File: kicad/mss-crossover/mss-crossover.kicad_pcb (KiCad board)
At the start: 2 copper layers, 73.7 x 38.1 mm, 40 parts, among them J1 Screw_Terminal_01x02, J2 AVR-ISP, J3 8P8C, J4 8P8C, SW1 FSM4JSMATR, T1 PE-51687, U1 AP7381-33Y, U2 INA180A4, U3 ATtiny85-20S, U4 TLP241A

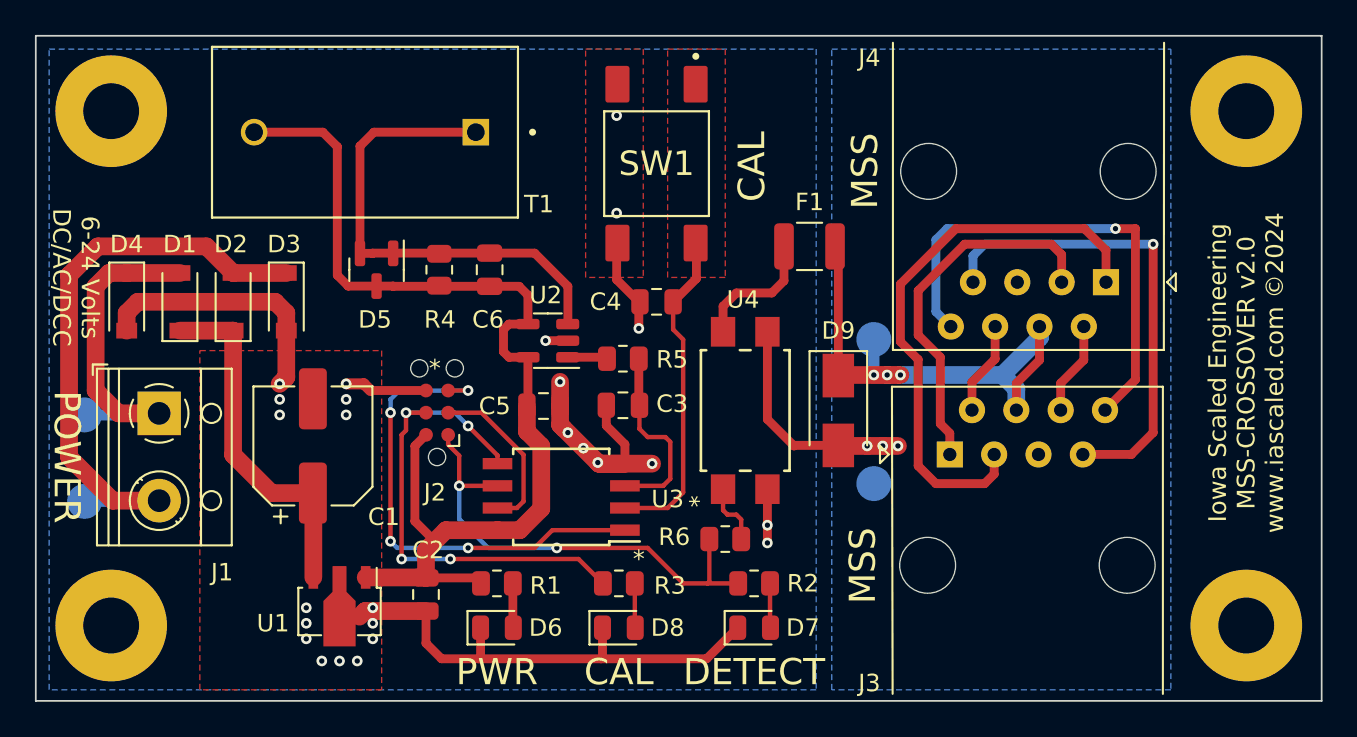
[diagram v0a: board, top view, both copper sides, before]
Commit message: Update footprints for AVR to allow for both narrow/wide SO8s and footprint for CDBMs to allow for more paste
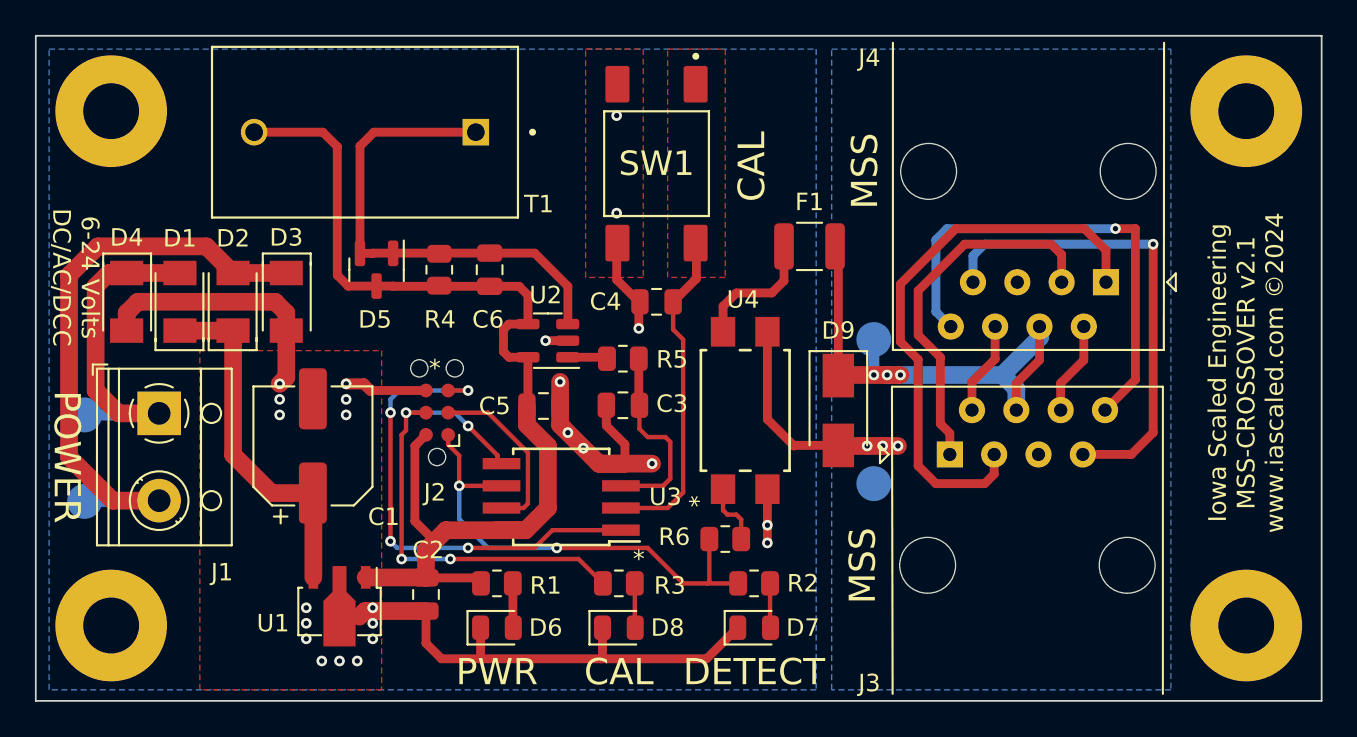
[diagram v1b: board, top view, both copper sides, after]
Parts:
- D1, D2, D3, D4: footprint Diode_SMD:D_SOD-123 -> ISE_Generic:SOD-123T
- U3: footprint Package_SO:SOIC-8W_5.3x5.3mm_P1.27mm -> ISE_Generic:ATMEL_SO8_DUAL
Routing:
- net +3.3V: track 61.5 -> 63.1 mm
- net GND: vias 26 -> 25
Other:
- board text added: "Iowa Scaled Engineering MSS-CROSSOVER v2.1 www.iascaled.com ©2024"
- board text removed: "Iowa Scaled Engineering MSS-CROSSOVER v2.0 www.iascaled.com ©2024"

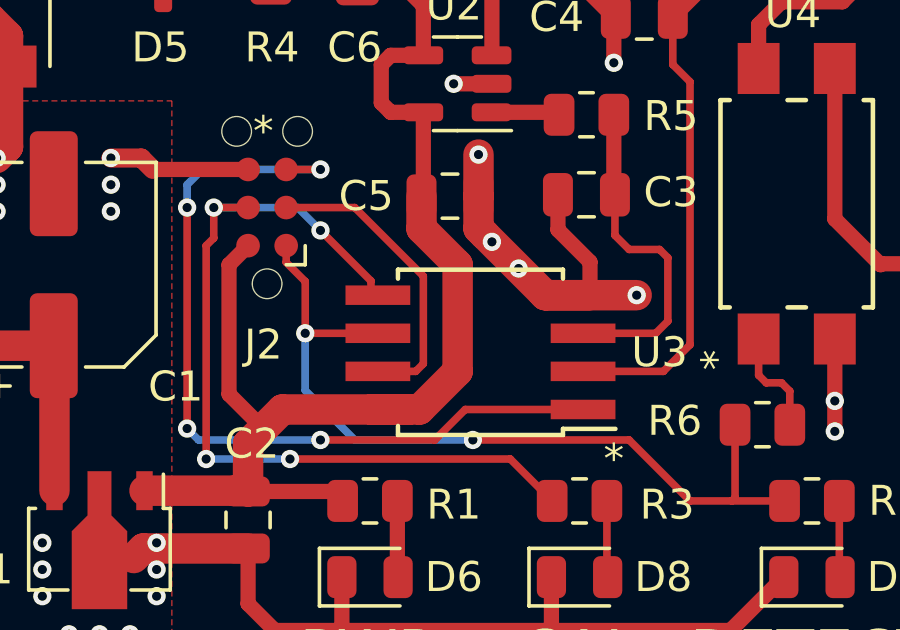
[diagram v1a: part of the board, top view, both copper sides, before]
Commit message: Fix dual footprint SO8
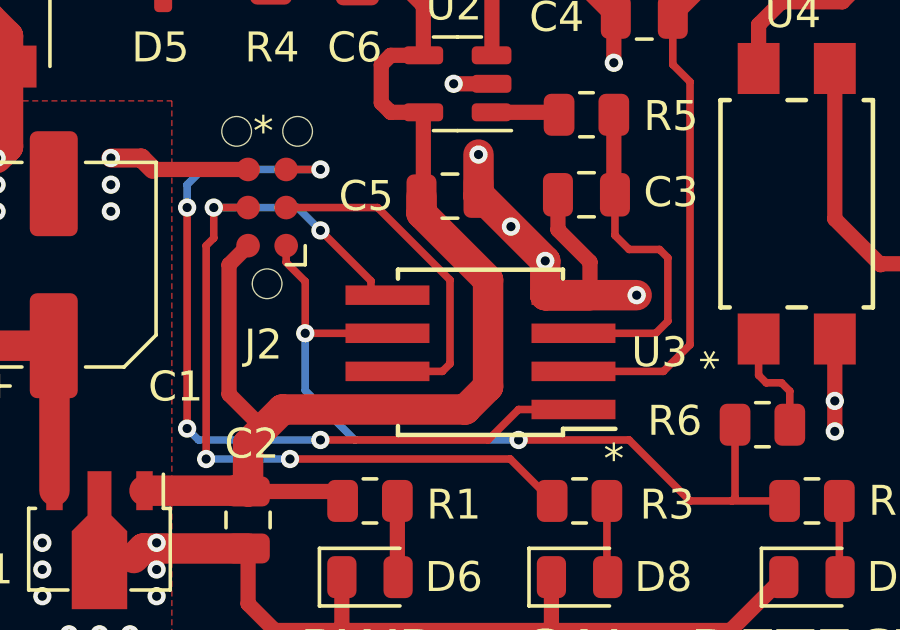
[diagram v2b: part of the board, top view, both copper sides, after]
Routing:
- net Net-(J2-Pad3): track 10.1 -> 12.7 mm
- net +3.3V: track 63.1 -> 63.8 mm

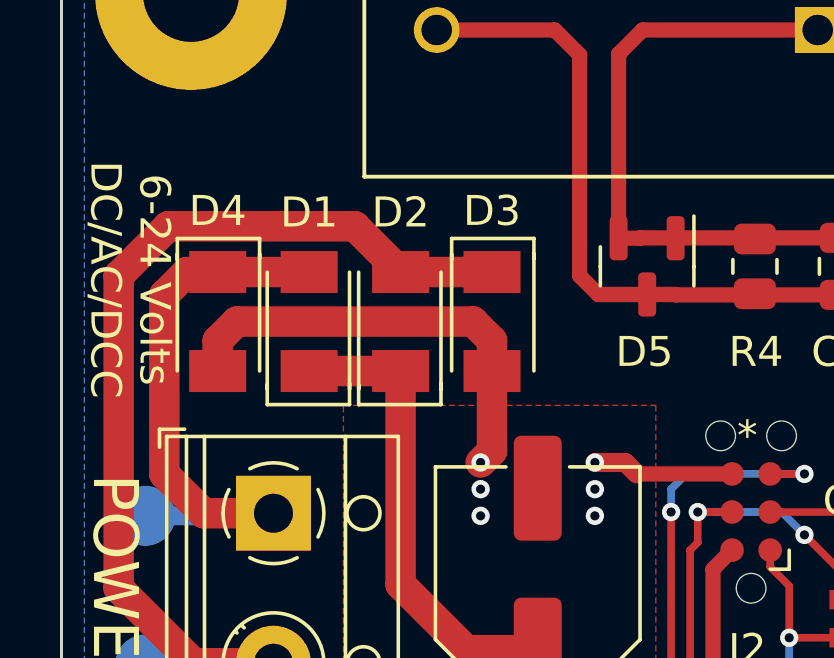
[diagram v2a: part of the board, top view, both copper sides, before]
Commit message: Fix diode spacing to appease McFussyPants
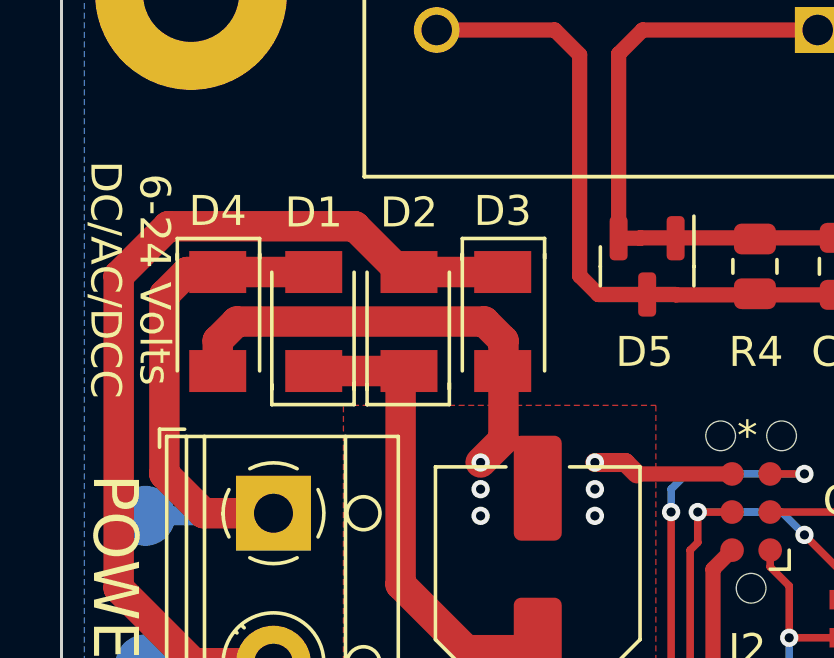
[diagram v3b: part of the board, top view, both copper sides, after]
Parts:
- moved D3 0.36 mm to (40.1, 168.9)
- moved D2 0.28 mm to (37.0, 168.9)
- moved D1 0.15 mm to (33.8, 168.9)
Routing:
- net GND: track 71.5 -> 72.1 mm
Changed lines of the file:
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@@
   )
   (footprint "ISE_Generic:SOD-123T" (layer "F.Cu")
-    (at 36.703 168.91 90)
+    (at 36.9824 168.91 90)
     (descr "SOD-123")
     (tags "SOD-123")
@@
   )
   (footprint "ISE_Generic:SOD-123T" (layer "F.Cu")
-    (at 33.655 168.91 90)
+    (at 33.8074 168.91 90)
     (descr "SOD-123")
     (tags "SOD-123")
@@
   )
   (footprint "ISE_Generic:SOD-123T" (layer "F.Cu")
-    (at 39.751 168.91 -90)
+    (at 40.1066 168.91 -90)
     (descr "SOD-123")
     (tags "SOD-123")
@@
   (segment (start 55.433 174.879) (end 55.433 173.4935) (width 1.016) (layer "F.Cu") (net 2))
   (segment (start 55.499 174.879) (end 57.658 177.038) (width 1.016) (layer "F.Cu") (net 2))
-  (segment (start 39.751 173.228) (end 39.37 173.609) (width 1.016) (layer "F.Cu") (net 2))
   (segment (start 67.31 182.72125) (end 67.31 179.73675) (width 0.508) (layer "F.Cu") (net 2))
   (segment (start 47.752 186.624) (end 47.752 188.468) (width 0.508) (layer "F.Cu") (net 2))
   (segment (start 47.752 188.468) (end 48.641 189.357) (width 0.508) (layer "F.Cu") (net 2))
   (segment (start 58.674 167.64) (end 58.674 165.591) (width 0.508) (layer "F.Cu") (net 2))
-  (segment (start 39.751 170.56) (end 39.751 173.228) (width 1.016) (layer "F.Cu") (net 2))
+  (segment (start 39.497 168.91) (end 40.132 169.545) (width 1.016) (layer "F.Cu") (net 2))
   (segment (start 58.0815 176.0035) (end 59.149 177.071) (width 0.508) (layer "F.Cu") (net 2))
-  (segment (start 31.242 168.91) (end 39.116 168.91) (width 1.016) (layer "F.Cu") (net 2))
   (segment (start 59.944 170.434) (end 59.944 168.976) (width 0.508) (layer "F.Cu") (net 2))
   (segment (start 59.149 177.071) (end 59.149 178.181) (width 0.508) (layer "F.Cu") (net 2))
   (segment (start 47.752 173.99) (end 44.577 173.99) (width 0.508) (layer "F.Cu") (net 2))
   (segment (start 44.262 186.624) (end 43.942 186.944) (width 1.016) (layer "F.Cu") (net 2))
+  (segment (start 31.242 168.91) (end 39.497 168.91) (width 1.016) (layer "F.Cu") (net 2))
   (segment (start 59.944 168.91) (end 58.674 167.64) (width 0.508) (layer "F.Cu") (net 2))
+  (segment (start 40.132 172.847) (end 39.37 173.609) (width 1.016) (layer "F.Cu") (net 2))
   (segment (start 57.658 178.181) (end 59.149 178.181) (width 1.016) (layer "F.Cu") (net 2))
-  (segment (start 30.607 170.56) (end 30.607 169.545) (width 1.016) (layer "F.Cu") (net 2))
   (segment (start 63.8325 189.357) (end 65.6105 187.579) (width 0.508) (layer "F.Cu") (net 2))
-  (segment (start 39.751 169.545) (end 39.751 170.56) (width 1.016) (layer "F.Cu") (net 2))
+  (segment (start 30.607 170.56) (end 30.607 169.545) (width 1.016) (layer "F.Cu") (net 2))
+  (segment (start 30.607 169.545) (end 31.242 168.91) (width 1.016) (layer "F.Cu") (net 2))
   (segment (start 50.8785 187.579) (end 50.8785 189.2785) (width 0.508) (layer "F.Cu") (net 2))
   (segment (start 57.658 177.038) (end 57.658 178.181) (width 1.016) (layer "F.Cu") (net 2))
-  (segment (start 39.116 168.91) (end 39.751 169.545) (width 1.016) (layer "F.Cu") (net 2))
   (segment (start 57.8635 189.2785) (end 57.785 189.357) (width 0.508) (layer "F.Cu") (net 2))
   (segment (start 44.196 173.609) (end 44.577 173.99) (width 0.635) (layer "F.Cu") (net 2))
   (segment (start 55.433 174.879) (end 55.499 174.879) (width 1.016) (layer "F.Cu") (net 2))
+  (segment (start 40.132 169.545) (end 40.132 172.847) (width 1.016) (layer "F.Cu") (net 2))
   (segment (start 47.752 186.624) (end 44.262 186.624) (width 1.016) (layer "F.Cu") (net 2))
   (segment (start 50.8785 189.2785) (end 50.8 189.357) (width 0.508) (layer "F.Cu") (net 2))
@@
   (segment (start 60.706 178.181) (end 57.658 178.181) (width 1.016) (layer "F.Cu") (net 2))
   (segment (start 57.8635 187.579) (end 57.8635 189.2785) (width 0.508) (layer "F.Cu") (net 2))
-  (segment (start 30.607 169.545) (end 31.242 168.91) (width 1.016) (layer "F.Cu") (net 2))
   (segment (start 57.785 189.357) (end 63.8325 189.357) (width 0.508) (layer "F.Cu") (net 2))
   (segment (start 48.641 189.357) (end 50.8 189.357) (width 0.508) (layer "F.Cu") (net 2))

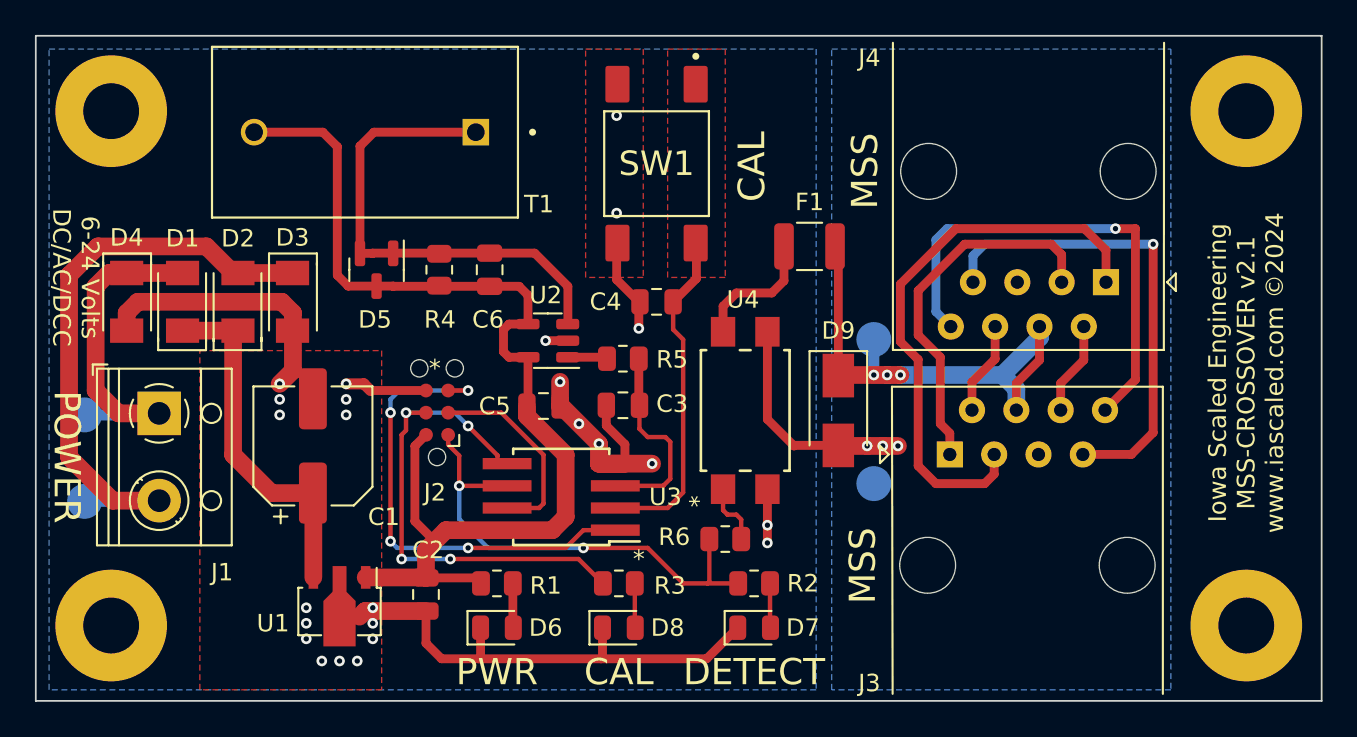
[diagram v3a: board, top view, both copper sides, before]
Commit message: Add auxilliary detection terminal block
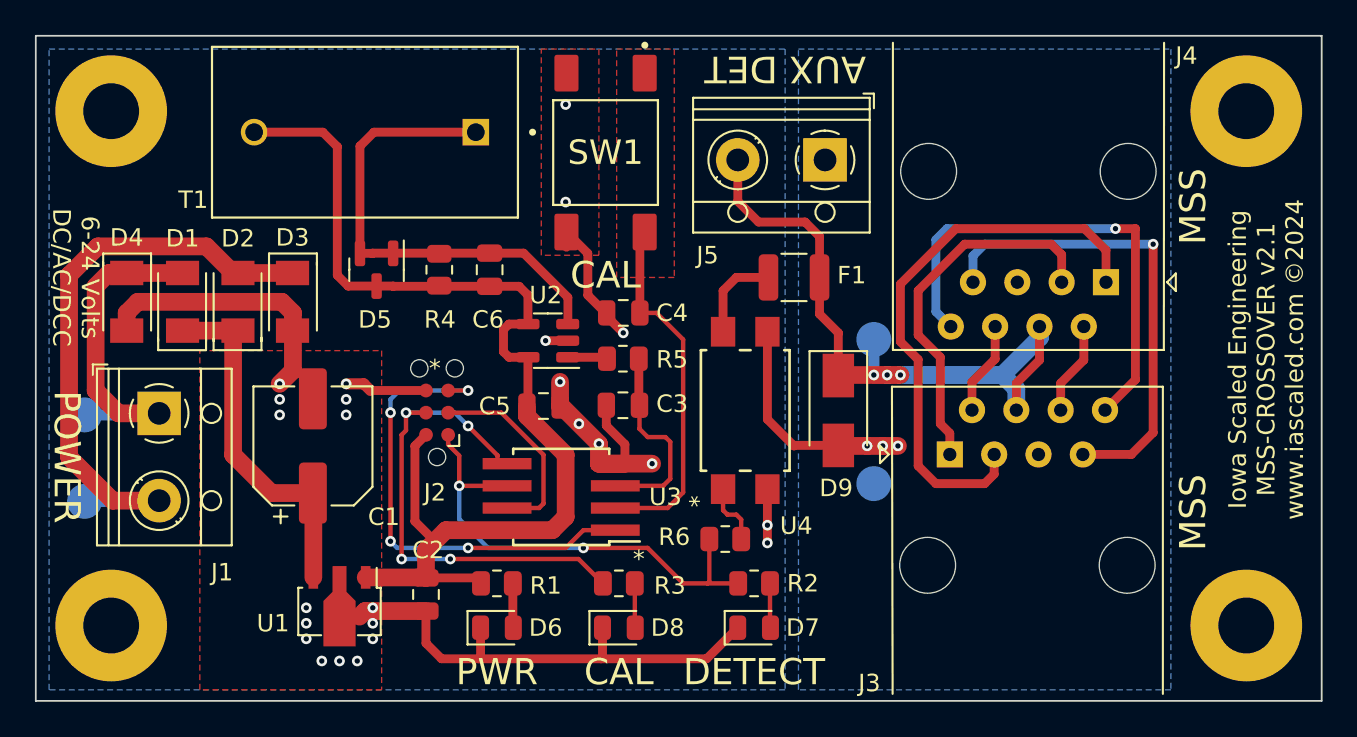
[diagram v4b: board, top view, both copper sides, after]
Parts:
- added J5: Screw_Terminal_01x02, TerminalBlock_RND:TerminalBlock_RND_205-00012_1x02_P5.00mm_Horizontal, F.Cu at (70.6, 160.8)
- moved SW1 2.99 mm to (58.0, 160.4)
- moved C4 2.01 mm to (59.1, 169.5)
- moved F1 1.99 mm to (68.8, 167.5)
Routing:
- net /MSS_OCC: track 31.5 -> 40.6 mm
- net GND: track 72.1 -> 74.8 mm
- net Net-(F1-Pad2): track 7.53 -> 5.27 mm
- net /~{CAL_SW}: track 18.7 -> 20.3 mm
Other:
- board text added: "AUX DET"

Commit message: Move transformer over and center switch to give more finger room Label aux detect terminals for GND and IN
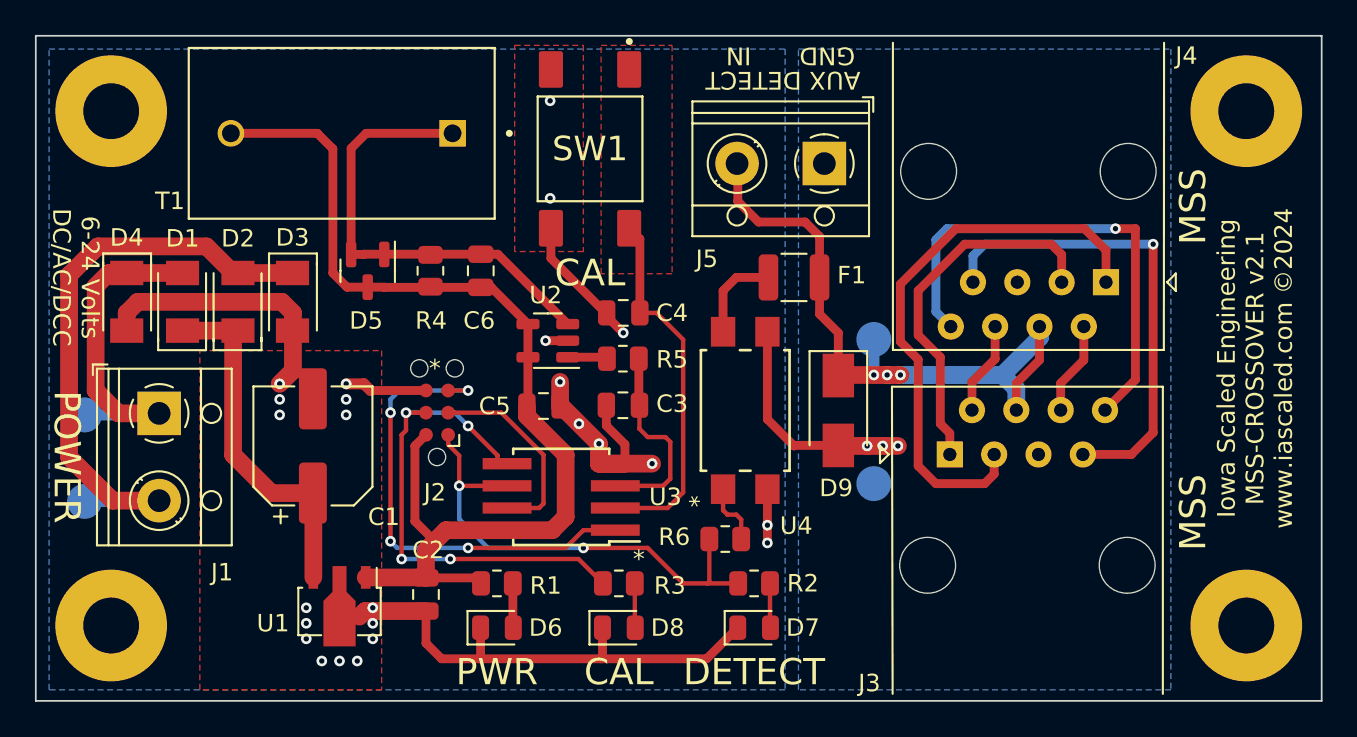
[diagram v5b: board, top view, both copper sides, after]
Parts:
- moved T1 1.33 mm to (42.9, 159.3)
- moved SW1 0.91 mm to (57.1, 160.1)
- moved D5 0.51 mm to (44.4, 167.1)
- moved R4 0.51 mm to (48.0, 167.1)
- moved C6 0.51 mm to (50.9, 167.1)
- moved J5 0.21 mm to (70.6, 161.0)
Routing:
- net +3.3V: track 63.8 -> 61.8 mm
- net Net-(C6-Pad1): track 27.6 -> 26.1 mm
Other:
- board text added: "AUX DETECT"
- board text added: "GND"
- board text added: "IN"
- board text removed: "AUX DET"
